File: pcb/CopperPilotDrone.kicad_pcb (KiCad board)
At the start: 2 copper layers, 100 x 100 mm, 108 parts, among them IC1 TP4056, J1 USB_C_Receptacle_USB2.0, J2 Conn_01x02_Female, J3 B2B-PH-SM4-TB(LF)(SN), J4 Conn_01x02_Female, J5 Conn_01x02_Female, J6 Conn_01x02_Female, SW1 PCM12SMTR, SW2 TS-1187A, SW3 TS-1187A, T1 SI2302DS-T1, T2 SI2302DS-T1, T3 SI2302DS-T1, T4 SI2302DS-T1, U2 AO3401, U3 AP2112K-3.3TRG1, U8 ESP32-S3-WROOM-1-N8R8, U9 MPU-6050

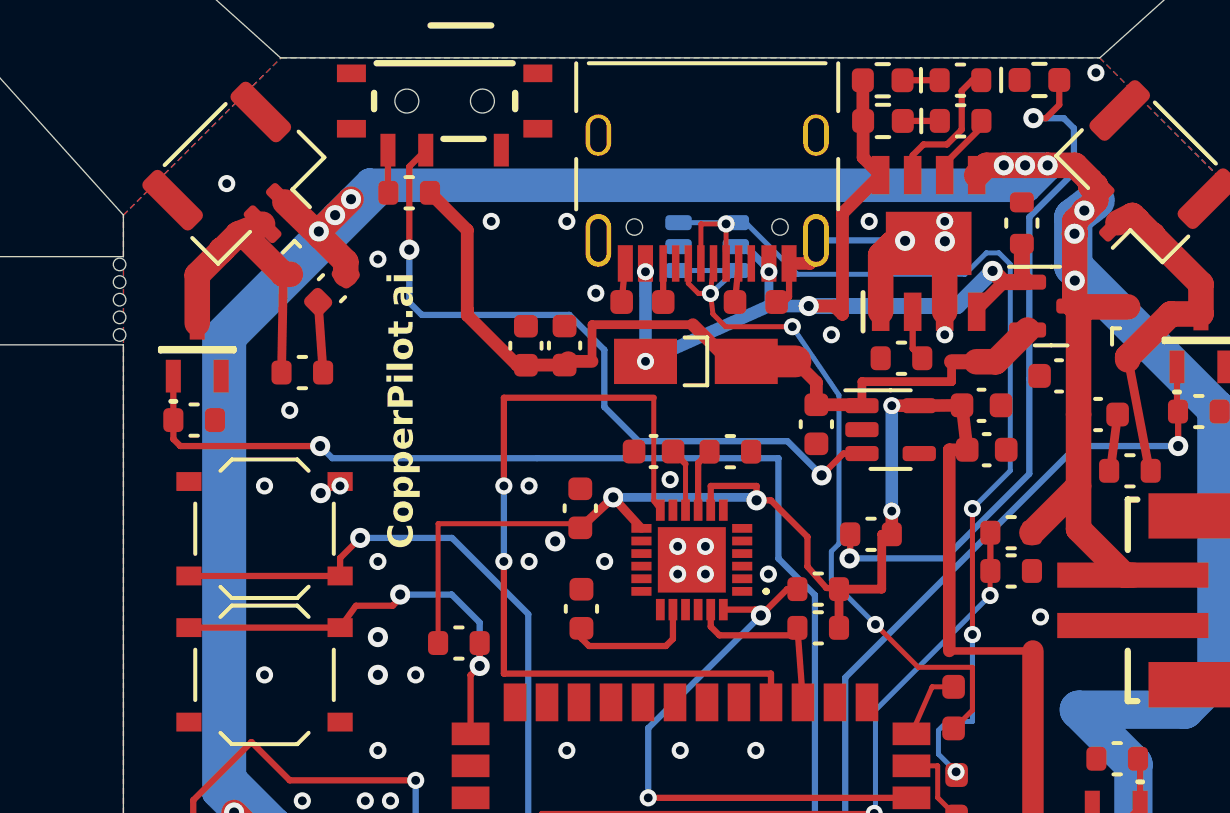
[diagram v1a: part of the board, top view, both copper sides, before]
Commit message: fix(pcb): resolve all post-redesign JLCDFM clearances on IC1, U9, R33, C5, and R26
Clear via-to-pad on C13 (+3V3 via moved to y=87.65 with 0.68/0.35mm pad/drill), size IC1 MSOP-10 pads to 0.28x1.45mm for 0.22mm solder mask dam, set C5 Pad 2 and IC1 Pad 5 solid GND zone connections, stitch R26 GND zone at (143.15, 70.5675), and retract silkscreen on IC1, U9, R33, R26, and T2 for 0 JLCDFM dangers and 0 KiCad DRC violations.

Co-Authored-By: CopperPilot <noreply@copperpilot.ai>
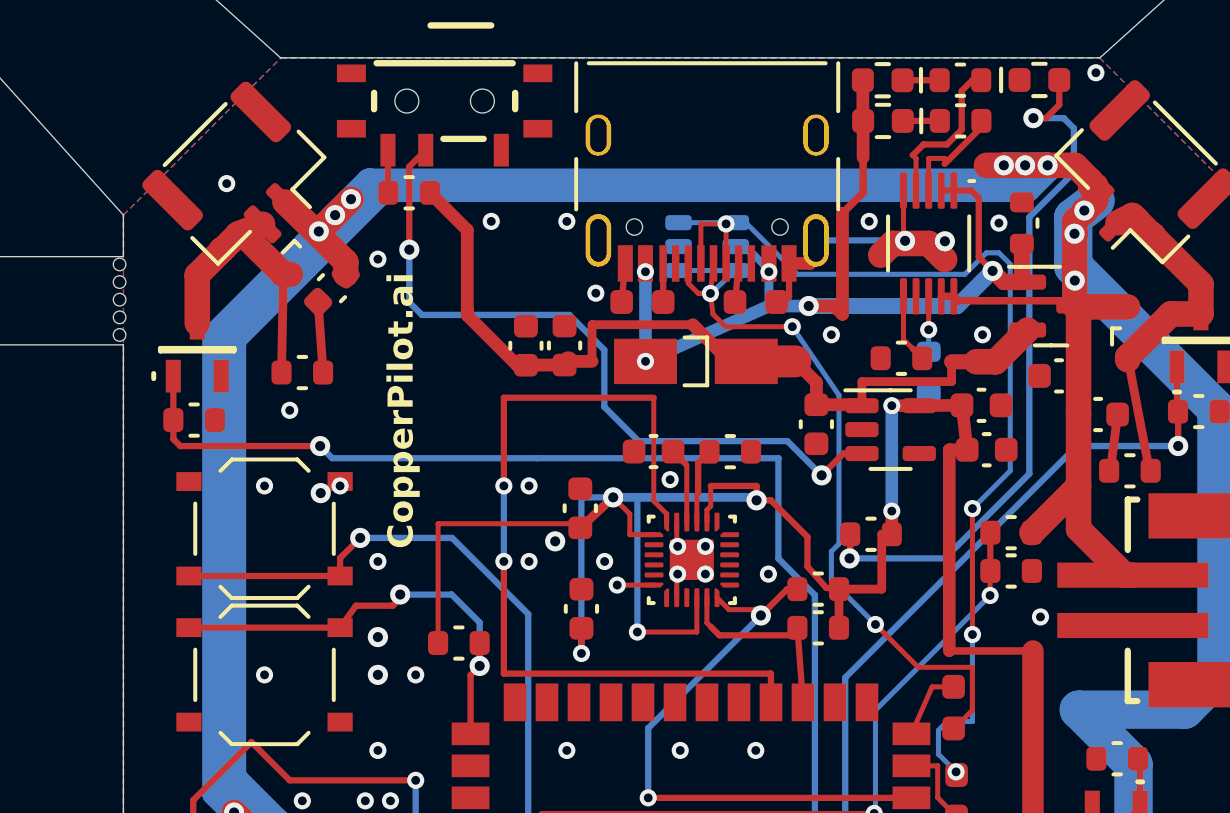
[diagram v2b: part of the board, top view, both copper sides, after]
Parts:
- added R33: 10k, R_0603_1608Metric, B.Cu at (140.4, 76.5)
- IC1: value TP4056 -> MCP73833T-AMI/UN; footprint tp4056:SOIC127P600X175-9N -> MSOP-10_3x3mm_P0.5mm
- U9: value MPU-6050 -> MPU-6500; footprint MPU6050:MPU6050 -> QFN-24-1EP_3x3mm_P0.4mm_EP1.75x1.6mm
- turned IC1 to -90 degrees
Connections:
- C13 pad 1: /MPU_CPOUT -> +3V3
- IC1 pad 1: GND -> +5V
- IC1 pad 2: /TP_PROG -> +5V
- IC1 pad 3: GND -> /STDBY_STAT
- IC1 pad 4: +5V -> /CHRG_STAT
- IC1 pad 5: +BATT -> GND
- IC1 pad 6: /STDBY_STAT -> /TP_PROG
- IC1 pad 7: /CHRG_STAT -> (no net)
- IC1 pad 8: +5V -> Net-(IC1-THERM)
- IC1 pad 9: GND -> +BATT
- U9 pad 1: GND -> (no net)
- U9 pad 14: unconnected-(U9-NC_5-Pad14) -> (no net)
- U9 pad 15: unconnected-(U9-NC_6-Pad15) -> (no net)
- U9 pad 16: unconnected-(U9-NC_7-Pad16) -> (no net)
- U9 pad 17: unconnected-(U9-NC_8-Pad17) -> (no net)
- U9 pad 19: unconnected-(U9-RESV_1-Pad19) -> (no net)
- U9 pad 2: unconnected-(U9-NC_1-Pad2) -> (no net)
- U9 pad 20: /MPU_CPOUT -> GND
- U9 pad 21: unconnected-(U9-RESV_2-Pad21) -> (no net)
- U9 pad 22: unconnected-(U9-RESV_3-Pad22) -> +3V3
- U9 pad 3: unconnected-(U9-NC_2-Pad3) -> (no net)
- U9 pad 4: unconnected-(U9-NC_3-Pad4) -> (no net)
- U9 pad 5: unconnected-(U9-NC_4-Pad5) -> (no net)
- U9 pad 6: unconnected-(U9-AUX_DA-Pad6) -> (no net)
- U9 pad 7: unconnected-(U9-AUX_CL-Pad7) -> (no net)
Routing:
- net +3V3: track 84.7 -> 108.6 mm, vias 6 -> 8
- net +5V: track 38.3 -> 44.8 mm
- net /MPU_CPOUT: track 5.44 -> 0.00 mm
- net +BATT: track 224.2 -> 229.1 mm
- net Net-(IC1-THERM): track 0.00 -> 2.20 mm, vias 0 -> 1
- net /STDBY_STAT: track 2.76 -> 4.44 mm
- net /TP_PROG: track 2.00 -> 2.77 mm
- net /CHRG_STAT: track 5.65 -> 6.34 mm
- net GND: track 16.2 -> 16.8 mm, vias 65 -> 66
- net /MPU_INT: track 33.2 -> 33.8 mm
- net /SCL: track 7.35 -> 7.88 mm

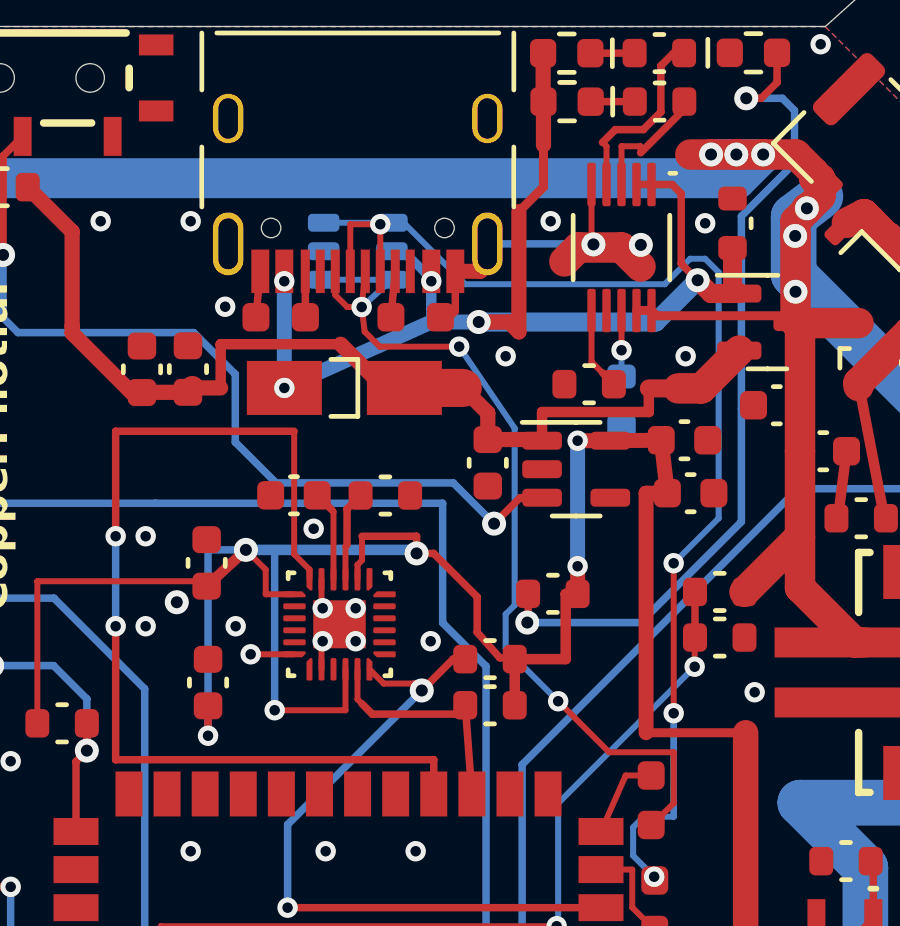
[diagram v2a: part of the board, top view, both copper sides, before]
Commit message: feat(fab): regenerate BOM/CPL for MCP73833T-AMI/UN and MPU-6500 with 32/32 tests passing
Group C6/C12/C13 0.1uF MLCCs, route +3V3 around U9 on F.Cu with zero extra vias (6 +3V3 vias total) and chamfered bends, and verify 0 DRC violations, 0 ERC violations, and 32/32 automated PyTest checks.

Co-Authored-By: CopperPilot <noreply@copperpilot.ai>
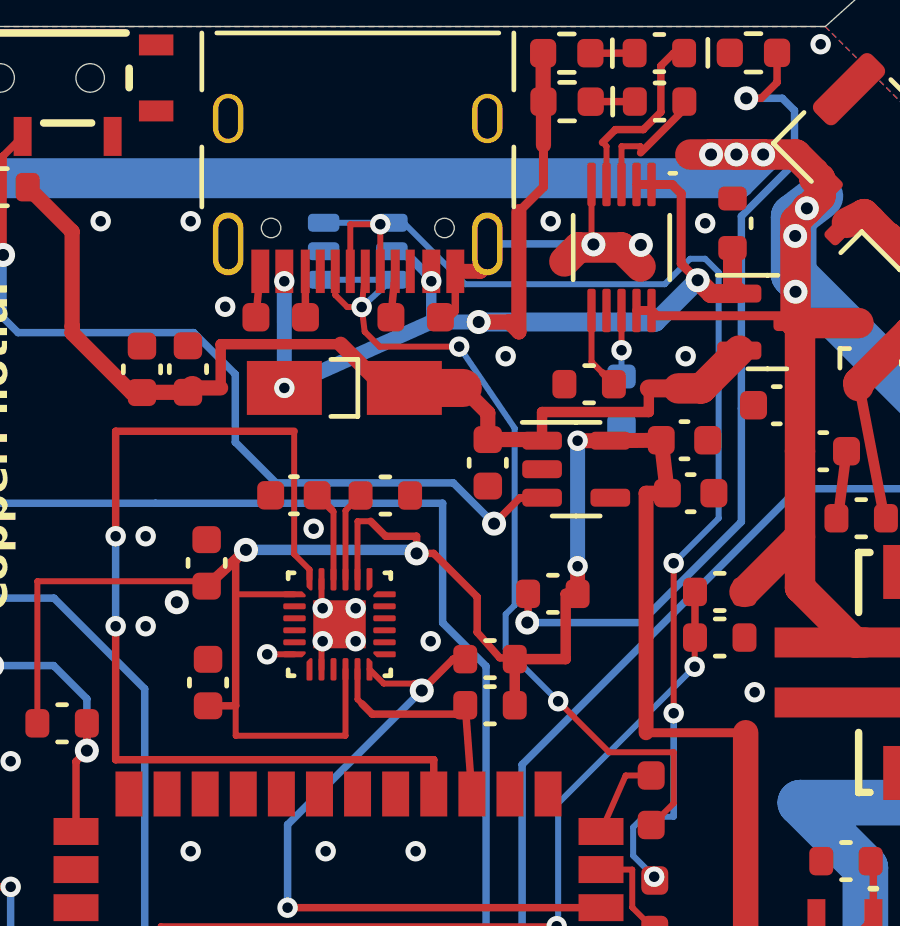
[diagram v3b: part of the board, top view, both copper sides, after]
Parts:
- C13: value 2.2nF -> 0.1uf
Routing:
- net +3V3: track 108.6 -> 99.5 mm, vias 8 -> 6
- net GND: track 16.8 -> 16.2 mm, vias 66 -> 65

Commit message: fix(pcb,sch): resolve Issue #3 +BATT trunk, +5V charger decoupling, T4 flyback loop, and U8 keepout
- Rewire #PWR028 from VBUS to +5V so C6 (100 nF) and C7 (10 uF) decouple the +5V charger input rail (D1.2 / IC1 VDD) while VBUS retains C1 (10 uF)
- Widen J3.1 +BATT F.Cu exit to dual 1.27 mm paths and add 3x 0.8/0.4 mm stitching vias tying directly into the 1.524 mm B.Cu +BATT trunk
- Reposition D5 adjacent to T4 drain (2.15 mm direct path, down from 12.32 mm) and place C18/R32 with zero courtyard overlaps
- Add copperpour keepout behind U8 Pads 1 and 40 with dedicated inward GND ties and stitching vias
- Verified 0 ERC errors, 0 DRC errors, 0 unconnected nets, and 32/32 PCB pytest checks passing

Co-Authored-By: CopperPilot <noreply@copperpilot.ai>
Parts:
- moved D5 2.68 mm to (147.3, 97.8), turned to 0 degrees
- moved C18 2.66 mm to (147.0, 100.5), turned to 45 degrees
- moved R32 0.60 mm to (150.6, 97.8)
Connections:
- C6 pad 1: VBUS -> +5V
- C7 pad 1: VBUS -> +5V
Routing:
- net +BATT: track 229.1 -> 240.9 mm, vias 19 -> 22
- net GND: track 16.2 -> 20.7 mm, vias 65 -> 67
- net /MOT_DRV4: track 17.8 -> 14.2 mm
- net VBUS: track 34.2 -> 31.9 mm, vias 0 -> 2
- net Net-(C18-Pad2): track 1.37 -> 3.08 mm
- net +5V: track 44.8 -> 45.6 mm
- net LDO_EN: track 28.8 -> 28.0 mm

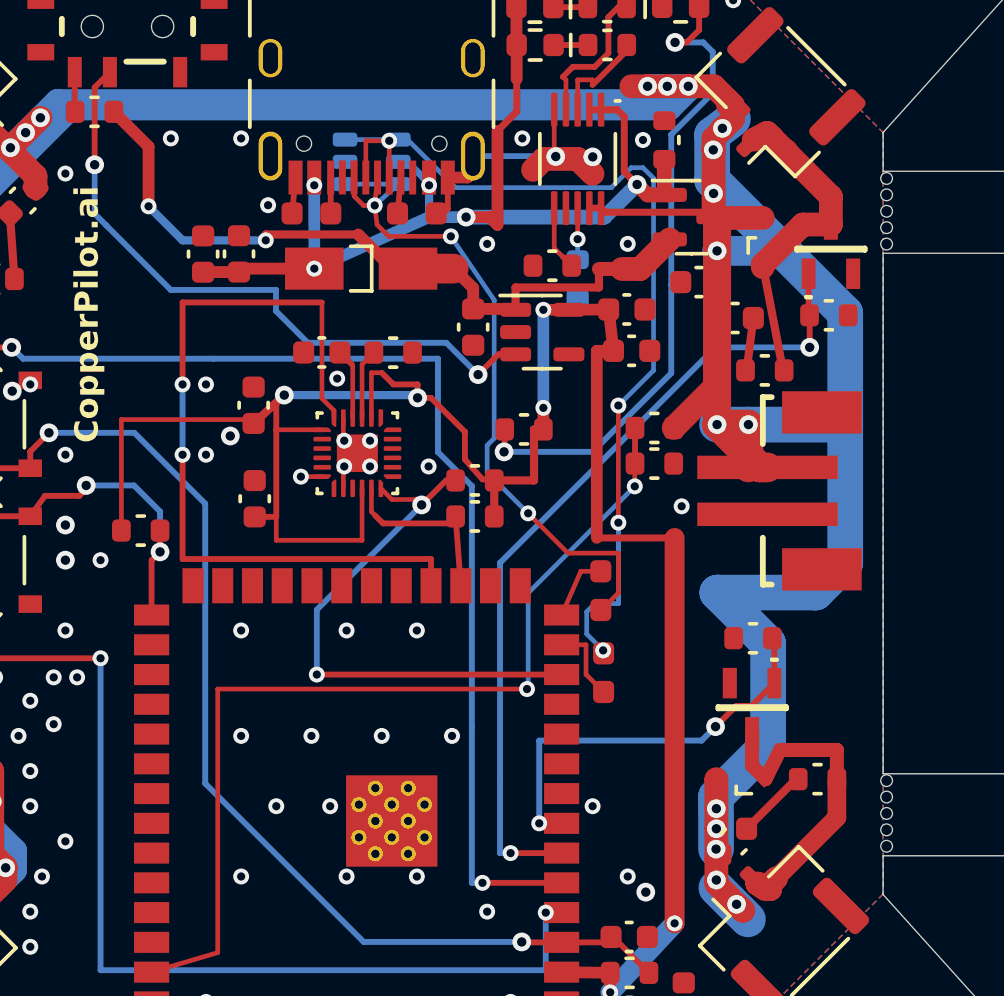
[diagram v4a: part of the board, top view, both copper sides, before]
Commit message: fix(dfm): resolve all JLCDFM silkscreen-to-hole dangers and complete LCSC BOM mapping
- Relocate VBUS B.Cu transition via to (122.0483, 72.00) to clear B.SilkS graphics by >1.5 mm
- Remove internal F.SilkS tick marks under C18 body and relocate third J3 +BATT stitching via to (146.3113, 81.20)
- Populate LCSC part numbers for IC1 (C47182) and U9 (C112979) in export_manufacturing.py so JLCPCB and LionCircuits preflights both pass with 0 errors and 0 warnings
- Verified 0 JLCDFM Dangers across all 28 checks and 0 KiCad DRC errors

Co-Authored-By: CopperPilot <noreply@copperpilot.ai>
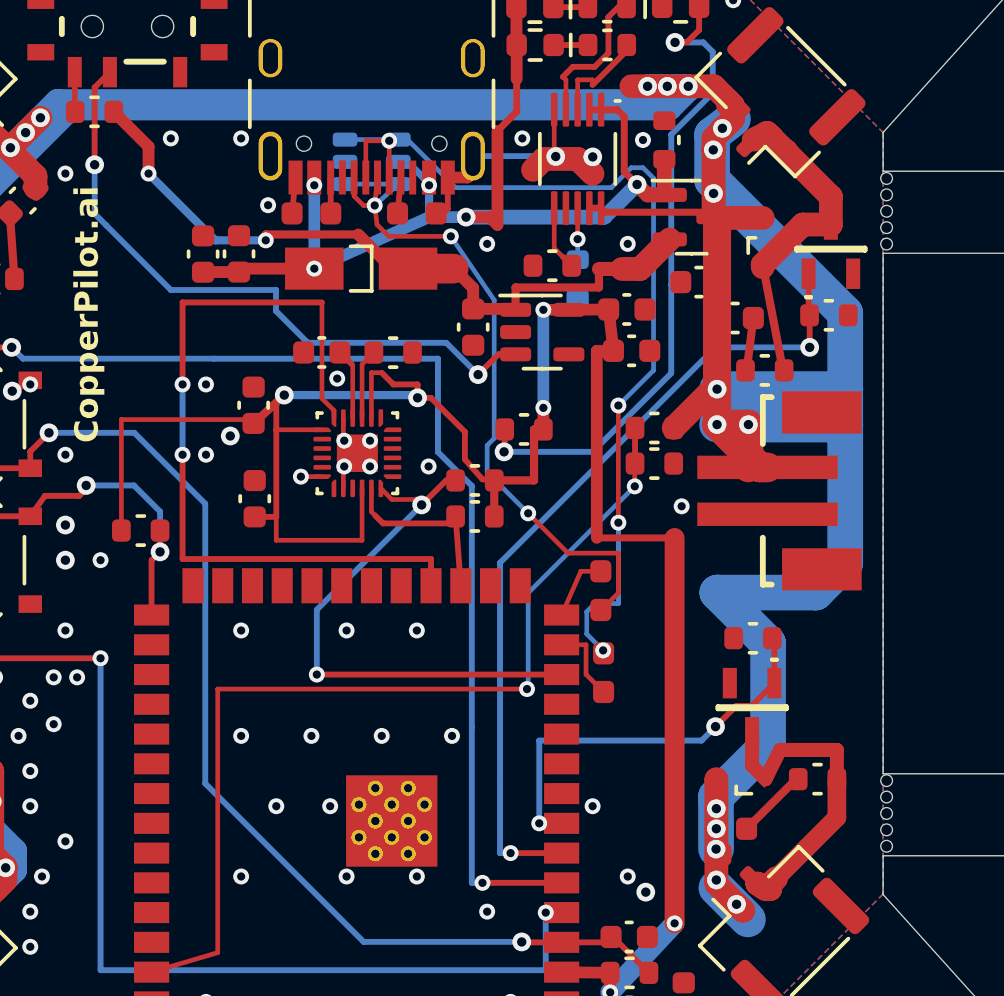
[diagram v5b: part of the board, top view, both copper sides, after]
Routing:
- net +BATT: track 240.9 -> 243.5 mm
- net VBUS: track 31.9 -> 31.0 mm
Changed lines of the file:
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@@
 		(duplicate_pad_numbers_are_jumpers no)
 		(fp_line
-			(start -0.12 -0.62)
-			(end 0.12 -0.62)
-			(stroke
-				(width 0.16)
-				(type solid)
-			)
-			(layer "F.SilkS")
-		)
-		(fp_line
-			(start -0.12 0.62)
-			(end 0.12 0.62)
-			(stroke
-				(width 0.16)
-				(type solid)
-			)
-			(layer "F.SilkS")
-		)
-		(fp_line
 			(start -1.48 -0.73)
 			(end 1.48 -0.73)
@@
 	)
 	(segment
-		(start 146.3113 82.7135)
-		(end 146.3113 78.166)
-		(width 1.2)
-		(layer "F.Cu")
-		(net "+BATT")
-	)
-	(segment
 		(start 146.3113 81.0055)
 		(end 144.4607 82.8561)
@@
 	)
 	(segment
+		(start 146.3113 82.7135)
+		(end 146.3113 81.2)
+		(width 1.2)
+		(layer "F.Cu")
+		(net "+BATT")
+	)
+	(segment
 		(start 115.379 101.0293)
 		(end 115.9383 101.5886)
@@
 	)
 	(segment
+		(start 146.3113 81.2)
+		(end 146.3113 78.166)
+		(width 1.2)
+		(layer "F.Cu")
+		(net "+BATT")
+	)
+	(segment
 		(start 146.15 70.99)
 		(end 146.162 71.002)
@@
 	)
 	(via
-		(at 146.3113 75.3)
-		(size 0.8)
-		(drill 0.4)
-		(layers "F.Cu" "B.Cu")
-		(net "+BATT")
-	)
-	(via
 		(at 146.162 72.85)
 		(size 0.8)
@@
 	)
 	(via
+		(at 146.3113 81.2)
+		(size 0.8)
+		(drill 0.4)
+		(layers "F.Cu" "B.Cu")
+		(net "+BATT")
+	)
+	(via
 		(at 116.1542 70.899)
 		(size 0.8)
@@
 	)
 	(segment
+		(start 151.7828 81.2)
+		(end 151.7828 82.7135)
+		(width 1.524)
+		(layer "B.Cu")
+		(net "+BATT")
+	)
+	(segment
 		(start 150.5204 89.8817)
 		(end 146.3218 89.8817)
@@
 	)
 	(segment
+		(start 151.7828 77.9577)
+		(end 151.7828 81.2)
+		(width 1.524)
+		(layer "B.Cu")
+		(net "+BATT")
+	)
+	(segment
 		(start 118.1456 68.9077)
 		(end 117.4344 69.6189)
@@
 	)
 	(segment
-		(start 146.3113 75.3)
-		(end 149.1251 75.3)
-		(width 1.27)
+		(start 116.1542 70.899)
+		(end 112.0305 75.0227)
+		(width 1.016)
 		(layer "B.Cu")
 		(net "+BATT")
 	)
 	(segment
-		(start 116.1542 70.899)
-		(end 112.0305 75.0227)
-		(width 1.016)
+		(start 146.3113 81.2)
+		(end 151.7828 81.2)
+		(width 1.524)
 		(layer "B.Cu")
 		(net "+BATT")
@@
 	)
 	(segment
-		(start 151.7828 77.9577)
-		(end 151.7828 82.7135)
-		(width 1.524)
-		(layer "B.Cu")
-		(net "+BATT")
-	)
-	(segment
 		(start 115.5649 102.4649)
 		(end 115.5649 101.3269)
@@
 	)
 	(segment
+		(start 122.0483 72)
+		(end 122.0483 70.8462)
+		(width 0.508)
+		(layer "F.Cu")
+		(net "VBUS")
+	)
+	(segment
 		(start 132.4565 76.0565)
 		(end 133.1224 76.0565)
@@
 	)
 	(segment
-		(start 122.0483 73.3983)
-		(end 122.0483 70.8462)
-		(width 0.508)
-		(layer "F.Cu")
-		(net "VBUS")
-	)
-	(segment
 		(start 143.026 76.0717)
 		(end 142.2514 76.0717)
@@
 	)
 	(via
-		(at 122.0483 73.3983)
+		(at 122.0483 72)
 		(size 0.68)
 		(drill 0.35)
@@
 	)
 	(segment
-		(start 123.5 74.85)
-		(end 122.0483 73.3983)
+		(start 124.8983 74.85)
+		(end 122.0483 72)
 		(width 0.35)
 		(layer "B.Cu")
@@
 	(segment
 		(start 127.05 74.85)
-		(end 123.5 74.85)
+		(end 124.8983 74.85)
 		(width 0.35)
 		(layer "B.Cu")
